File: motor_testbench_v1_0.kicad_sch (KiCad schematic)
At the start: 41 parts, among them IC1 PJA3402_R1_00001, J1 USB_C_Receptacle_USB2.0_16P, J3 Conn_02x06_Odd_Even, U1 ESP32-S3-WROOM-1, U3 ESP32-S3-DevKitC

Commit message: Add buffer OPA for Secondary battery measurement
[KiCad Version: 10.0.3]
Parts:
- removed J3: Conn_02x06_Odd_Even, Connector_PinHeader_2.00mm:PinHeader_2x06_P2.00mm_Vertical, symbol Connector_Generic:Conn_02x06_Odd_Even
- removed R56, R64, R65, R66: 22R, Resistor_SMD:R_0603_1608Metric_Pad0.98x0.95mm_HandSolder, symbol Device:R
- removed U3: ESP32-S3-DevKitC, custom_footprints:ESP32-S3-DevKitC_with_3DModel, symbol Espressif Symbols:ESP32-S3-DevKitC
- added C1, C134, C135, C5: 1u, Capacitor_SMD:C_0603_1608Metric_Pad1.08x0.95mm_HandSolder, symbol Device:C
- added C132: 10u, Capacitor_SMD:C_0603_1608Metric_Pad1.08x0.95mm_HandSolder, symbol Device:C
- added C6, C7, C8: 100n, Capacitor_SMD:C_0603_1608Metric_Pad1.08x0.95mm_HandSolder, symbol Device:C
- added D1, D2: GG040205170N2P, Diode_SMD:D_0402_1005Metric_Pad0.77x0.64mm_HandSolder, symbol Device:D
- added J2: Conn_02x08_Odd_Even, Connector_PinHeader_2.54mm:PinHeader_2x08_P2.54mm_Vertical, symbol Connector_Generic:Conn_02x08_Odd_Even
- added JP3: Jumper_2_Open, Jumper:SolderJumper-2_P1.3mm_Open_RoundedPad1.0x1.5mm, symbol Jumper:Jumper_2_Open
- added R1, R2: 5.1k, Resistor_SMD:R_0603_1608Metric_Pad0.98x0.95mm_HandSolder, symbol Device:R
- added R19, R20, R21, R3: 10k, Resistor_SMD:R_0603_1608Metric_Pad0.98x0.95mm_HandSolder, symbol Device:R
- added R73, R74: 22R, Resistor_SMD:R_0603_1608Metric_Pad0.98x0.95mm_HandSolder, symbol Device:R
- added SWd1, SWd4: SW_Push, Button_Switch_SMD:SW_SPST_TS-1088-xR020, symbol Switch:SW_Push
- added U21: OPA310SxDBV, Package_TO_SOT_SMD:SOT-23-6, symbol Amplifier_Operational:OPA310SxDBV
- renumbered C1 to C2, C2 to C3, C3 to C4, D1 to D3, R4 to R10, R59 to R11, R5 to R12, R7 to R14, R57 to R15, R67 to R16, R68 to R17, R69 to R18, R6 to R4, R60 to R5, R61 to R6, R1 to R7, R2 to R8, R3 to R9, SWd1 to SWd2, SWd2 to SWd3
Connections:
- net DS_ADC_MCLK is gone; now on net DS_ADC_IRQ: R15.2
- net +3V3_ESP: now also C5.1, J2.16 (Pin_16), R19.1, R20.1, R21.1, R3.1, U21.5 (~{SHDN})
- net ESP_EN/RST: now also SWd3.2, C7.1, R20.2
- net ESP_GPIO0: now also JP3.2 (B), R3.2, SWd4.2
- net ESP_GPIO1: now also C134.1, R74.2
- net ESP_GPIO11: now also J2.11 (Pin_11)
- net ESP_GPIO2: now also J2.15 (Pin_15)
- net ESP_GPIO38: now also J2.3 (Pin_3)
- net ESP_GPIO39: now also J2.2 (Pin_2)
- net ESP_GPIO40: now also J2.4 (Pin_4)
- net ESP_GPIO41: now also J2.6 (Pin_6)
- net ESP_GPIO42: now also J2.8 (Pin_8)
- net ESP_GPIO46: now also J2.9 (Pin_9)
- net ESP_GPIO9: now also C6.1, R19.2
- net ESP_UART_RX: now also J2.12 (Pin_12)
- net ESP_UART_TX: now also J2.10 (Pin_10)
- net ESP_USB_D+: now also D2.1 (K)
- net ESP_USB_D-: now also D1.1 (K)
- net GND: now also J1.SH (SHIELD), C1.2, C132.2, C134.2, C135.2, C5.2, C6.2, C7.2, C8.2, D1.2 (A), D2.2 (A), J2.1 (Pin_1), J2.14 (Pin_14), J2.5 (Pin_5), J2.7 (Pin_7), JP3.1 (A), R1.1, R2.1, SWd1.1, SWd4.1, U21.2 (V-)
- net V_secondary_Bat: now also U1.18 (IO10), C132.1, R73.2; no longer C4.1, R10.1, R9.2, U1.15 (IO3)
- net at J1.A4 (VBUS), J1.A9 (VBUS), J1.B4 (VBUS)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: now also C1.1
- net at J1.A5 (CC1): now also R1.2
- net at J1.B5 (CC2): now also R2.2
- removed net ESP_GPIO10: SWd3.2, U1.18 (IO10)
- new net: C4.1, R10.1, R9.2, U21.3 (+)
- new net: R73.1, U21.1, U21.4 (-)
- new net: J2.13 (Pin_13), R74.1
- new net +5V5_bus: C135.1, U21.6 (V+)
- new net ESP_GPIO3: C8.1, R21.2, SWd1.2, U1.15 (IO3)
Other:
- note added: "Extra Input Filter if ESP32 SAR ADC is used!"
- note added: "POISTA TAI TEE JOTAIN MCLK:LLE, EI VARMAAN TARVITA / EI VOI LAITTAA GPIO 45!"
- note added: "TARKASTA PINOUT: TLV9001SIDBVRG4"
- note removed: "ESP S3 DevKitC Header"
- moved on the sheet: C2, C3, C4, D3, J1, R10, R11, R12, R14, R15, R16, R17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

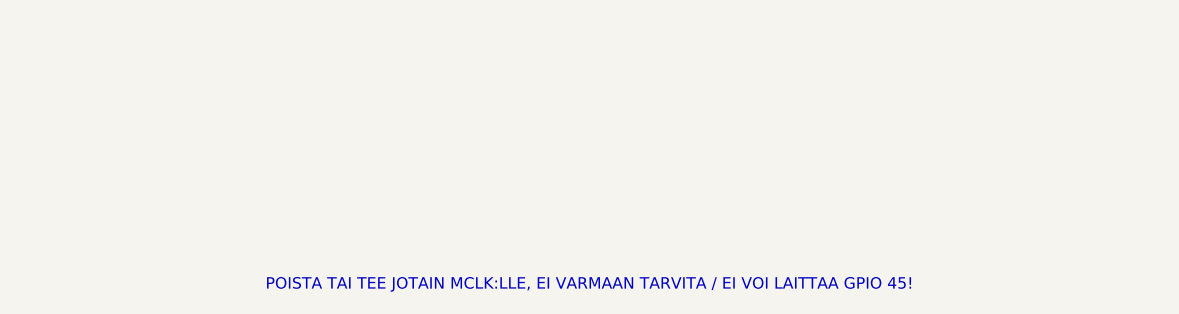
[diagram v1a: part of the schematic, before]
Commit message: Add LDO / Power sequencing for sensors
[KiCad Version: 10.0.3]
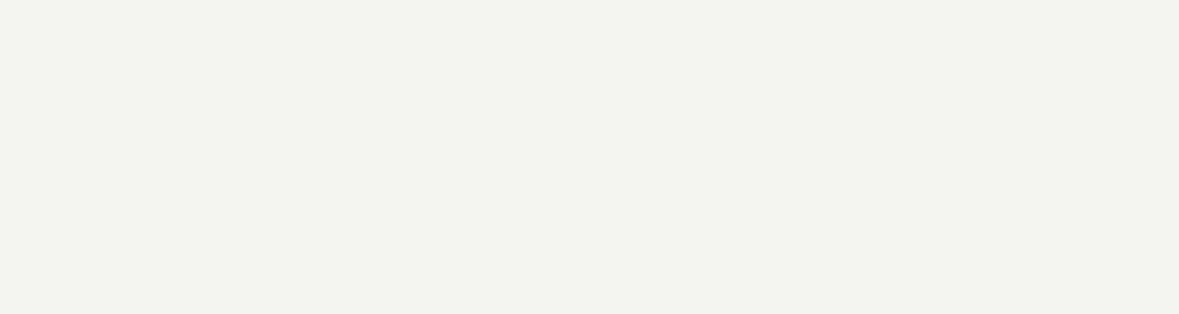
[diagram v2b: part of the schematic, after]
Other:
- note removed: "POISTA TAI TEE JOTAIN MCLK:LLE, EI VARMAAN TARVITA / EI VOI LAITTAA GPIO 45!"
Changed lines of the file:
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@@
-		)
-	)
-	(text "POISTA TAI TEE JOTAIN MCLK:LLE, EI VARMAAN TARVITA / EI VOI LAITTAA GPIO 45!"
-		(exclude_from_sim no)
-		(at 152.4 196.85 0)
-		(effects
-			(font
-				(size 1.27 1.27)
-			)
 		)
 	)

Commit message: Minor improvements. Add 3D model.
[KiCad Version: 10.0.4]
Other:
- moved on the sheet: C1, C132, C134, C135, C2, C3, C4, C5, C6, C7, C8, D1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

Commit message: Fix Via offset.
[KiCad Version: 10.0.4]
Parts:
- renumbered C2 to C1, C7 to C10, C8 to C11, C3 to C2, C5 to C3, C135 to C5, C1 to C6, C134 to C7, C132 to C8, C6 to C9, D3 to D1, D1 to D2, D2 to D3, JP3 to JP1, R3 to R1, R7 to R11, R16 to R12, R17 to R13, R18 to R14, R8 to R15, R1 to R16, R2 to R17, R74 to R18, R73 to R19, R4 to R2, R19 to R20, R20 to R21, R21 to R22, R5 to R3, R6 to R4, R11 to R5, R12 to R6, R14 to R7, R15 to R8, SWd4 to SWd1, SWd1 to SWd2, SWd2 to SWd3, SWd3 to SWd4, U21 to U2

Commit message: Minor improvements. Fix capacitor sizes.
[KiCad Version: 10.0.4]
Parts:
- removed H12, H9: MountingHole, MountingHole:MountingHole_2.2mm_M2_DIN965, symbol Mechanical:MountingHole
- added C3: 1u, Capacitor_SMD:C_0603_1608Metric_Pad1.08x0.95mm_HandSolder, symbol Device:C
- C5: renamed from C4; footprint Capacitor_SMD:C_0603_1608Metric_Pad1.08x0.95mm_HandSolder -> Capacitor_SMD:C_0805_2012Metric_Pad1.18x1.45mm_HandSolder
- C9: renamed from C8; footprint Capacitor_SMD:C_0603_1608Metric_Pad1.08x0.95mm_HandSolder -> Capacitor_SMD:C_0805_2012Metric_Pad1.18x1.45mm_HandSolder
- H1, H10, H11, H2, H3, H4, H5, H6, H7, H8: footprint MountingHole:MountingHole_2.2mm_M2_DIN965 -> MountingHole:MountingHole_3.2mm_M3
- IC1: footprint SOT95P240X110-3N -> SamacSys_Parts:SOT95P240X110-3N
- renumbered C9 to C10, C10 to C11, C11 to C12, C3 to C4, C5 to C6, C6 to C7, C7 to C8
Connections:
- net +3V3_ESP: now also J2.7 (Pin_7), C3.1
- net GND: now also C3.2; no longer J2.7 (Pin_7)
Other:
- moved on the sheet: C4

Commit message: PCB improvements.
[KiCad Version: 10.0.4]
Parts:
- removed J2: Conn_02x08_Odd_Even, Connector_PinHeader_2.54mm:PinHeader_2x08_P2.54mm_Vertical, symbol Connector_Generic:Conn_02x08_Odd_Even
- added J?: Conn_01x07_Pin, Connector_PinHeader_2.54mm:PinHeader_1x07_P2.54mm_Vertical, symbol Connector:Conn_01x07_Pin
- added J?: Conn_01x08_Pin, Connector_PinHeader_2.54mm:PinHeader_1x08_P2.54mm_Vertical, symbol Connector:Conn_01x08_Pin
- added TP (x3): TestPoint, TestPoint:TestPoint_Pad_D1.0mm, symbol Connector:TestPoint
- renumbered H11 to H10, H10 to H9
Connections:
- net +3V3_ESP: now also J?.5 (Pin_5), J?.8 (Pin_8)
- net ESP_GPIO11: now also J?.3 (Pin_3)
- net ESP_GPIO14: now also TP.1
- net ESP_GPIO2: now also J?.1 (Pin_1)
- net ESP_GPIO38: now also J?.7 (Pin_7)
- net ESP_GPIO39: now also J?.1 (Pin_1)
- net ESP_GPIO40: now also J?.2 (Pin_2)
- net ESP_GPIO41: now also J?.3 (Pin_3)
- net ESP_GPIO42: now also J?.4 (Pin_4)
- net ESP_GPIO46: now also J?.4 (Pin_4)
- net ESP_GPIO8: now also TP.1
- net ESP_UART_RX: now also J?.6 (Pin_6)
- net ESP_UART_TX: now also J?.5 (Pin_5)
- net GND: now also J?.6 (Pin_6), J?.7 (Pin_7), TP.1
- net at R18.1: now also J?.2 (Pin_2)
- no-connect marks 5 -> 6
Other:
- moved on the sheet: C3, C4

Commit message: PCB Improvements.
[KiCad Version: 10.0.4]
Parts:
- gave numbers to parts that had none: 2
- renumbered TP to TP1, TP to TP2, TP to TP3
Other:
- note added: "TODO: MAADOITA NÄMÄ?"
- note added: "TODO: TARKASTA PINOUT: TLV9001SIDBVRG4"
- note added: "TODO: VARMISTA ETTÄ PINNIT JA FOOTPRINT OIKEAT: PJA3402_R1_00001 SOT-23-3"
- note removed: "TARKASTA PINOUT: TLV9001SIDBVRG4"
- note removed: "VARMISTA ETTÄ PINNIT JA FOOTPRINT OIKEAT: PJA3402_R1_00001 SOT-23-3"
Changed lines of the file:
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@@
 		)
 	)
-	(text "Mechanical Mounting"
+	(text "TODO:\n\nVARMISTA ETTÄ PINNIT JA FOOTPRINT OIKEAT:\nPJA3402_R1_00001\nSOT-23-3\n"
 		(exclude_from_sim no)
-		(at 264.414 187.96 0)
+		(at 172.72 81.788 0)
 		(effects
 			(font
-				(size 1.27 1.27)
+				(size 1.905 1.905)
 			)
 		)
 	)
-	(text "TARKASTA PINOUT: TLV9001SIDBVRG4\n"
+	(text "Mechanical Mounting"
 		(exclude_from_sim no)
-		(at 220.98 62.23 0)
+		(at 264.414 187.96 0)
 		(effects
 			(font
@@
 		)
 	)
-	(text "VARMISTA ETTÄ PINNIT JA FOOTPRINT OIKEAT:\nPJA3402_R1_00001\nSOT-23-3\n"
+	(text "TODO: TARKASTA PINOUT: TLV9001SIDBVRG4\n"
 		(exclude_from_sim no)
-		(at 185.42 82.55 0)
+		(at 216.662 64.262 0)
 		(effects
 			(font
-				(size 1.27 1.27)
+				(size 1.905 1.905)
 			)
 		)
@@
 		)
 	)
+	(text "TODO: MAADOITA NÄMÄ?"
+		(exclude_from_sim no)
+		(at 277.622 215.9 0)
+		(effects
+			(font
+				(size 1.905 1.905)
+			)
+		)
+	)
 	(junction
 		(at 162.56 193.04)
@@
 		(dnp no)
 		(fields_autoplaced yes)
-		(property "Reference" "#PWR034"
+		(property "Reference" "#PWR035"
 			(at 264.16 130.81 0)
 			(hide yes)
@@
 			(project "motor_testbench_v1_0"
 				(path "/da638649-102c-44f9-b928-e91cd399cc2f"
-					(reference "#PWR034")
+					(reference "#PWR035")
 					(unit 1)
 				)
@@
 		(dnp no)
 		(fields_autoplaced yes)
-		(property "Reference" "#PWR026"
+		(property "Reference" "#PWR027"
 			(at 227.33 156.21 0)
 			(hide yes)
@@
 			(project "motor_testbench_v1_0"
 				(path "/da638649-102c-44f9-b928-e91cd399cc2f"
-					(reference "#PWR026")
+					(reference "#PWR027")
 					(unit 1)
 				)
@@
 		(in_pos_files yes)
 		(dnp no)
-		(property "Reference" "#PWR039"
+		(property "Reference" "#PWR040"
 			(at 280.67 147.32 0)
 			(hide yes)
@@
 			(project "motor_testbench_v1_0"
 				(path "/da638649-102c-44f9-b928-e91cd399cc2f"
-					(reference "#PWR039")
+					(reference "#PWR040")
 					(unit 1)
 				)
@@
 		(in_pos_files yes)
 		(dnp no)
-		(property "Reference" "TP"
+		(property "Reference" "TP2"
 			(at 41.91 158.75 0)
 			(hide yes)
@@
 			(project "motor_testbench_v1_0"
 				(path "/da638649-102c-44f9-b928-e91cd399cc2f"
-					(reference "TP")
+					(reference "TP2")
 					(unit 1)
 				)
@@
 		(in_pos_files yes)
 		(dnp no)
-		(property "Reference" "#PWR037"
+		(property "Reference" "#PWR038"
 			(at 280.67 113.03 0)
 			(hide yes)
@@
 			(project "motor_testbench_v1_0"
 				(path "/da638649-102c-44f9-b928-e91cd399cc2f"
-					(reference "#PWR037")
+					(reference "#PWR038")
 					(unit 1)
 				)
@@
 		(dnp no)
 		(fields_autoplaced yes)
-		(property "Reference" "#PWR016"
+		(property "Reference" "#PWR017"
 			(at 200.66 63.5 0)
 			(hide yes)
@@
 			(project "motor_testbench_v1_0"
 				(path "/da638649-102c-44f9-b928-e91cd399cc2f"
-					(reference "#PWR016")
+					(reference "#PWR017")
 					(unit 1)
 				)
@@
 		(in_pos_files yes)
 		(dnp no)
-		(property "Reference" "#PWR023"
+		(property "Reference" "#PWR024"
 			(at 223.52 55.88 0)
 			(hide yes)
@@
 			(project "motor_testbench_v1_0"
 				(path "/da638649-102c-44f9-b928-e91cd399cc2f"
-					(reference "#PWR023")
+					(reference "#PWR024")
 					(unit 1)
 				)
@@
 		(dnp no)
 		(fields_autoplaced yes)
-		(property "Reference" "J?"
+		(property "Reference" "J3"
 			(at 212.725 187.96 0)
 			(show_name no)
@@
 			(project "motor_testbench_v1_0"
 				(path "/da638649-102c-44f9-b928-e91cd399cc2f"
-					(reference "J?")
+					(reference "J3")
 					(unit 1)
 				)
@@
 		(in_pos_files yes)
 		(dnp no)
-		(property "Reference" "#PWR0247"
+		(property "Reference" "#PWR031"
 			(at 233.68 222.25 0)
 			(hide yes)
@@
 			(project "motor_testbench_v1_0"
 				(path "/da638649-102c-44f9-b928-e91cd399cc2f"
-					(reference "#PWR0247")
+					(reference "#PWR031")
 					(unit 1)
 				)
@@
 		(dnp no)
 		(fields_autoplaced yes)
-		(property "Reference" "#PWR036"
+		(property "Reference" "#PWR037"
 			(at 280.67 106.68 0)
 			(hide yes)
@@
 			(project "motor_testbench_v1_0"
 				(path "/da638649-102c-44f9-b928-e91cd399cc2f"
-					(reference "#PWR036")
+					(reference "#PWR037")
 					(unit 1)
 				)
@@
 		(in_pos_files yes)
 		(dnp no)
-		(property "Reference" "#PWR027"
+		(property "Reference" "#PWR028"
 			(at 227.33 273.05 0)
 			(hide yes)
@@
 			(project "motor_testbench_v1_0"
 				(path "/da638649-102c-44f9-b928-e91cd399cc2f"
-					(reference "#PWR027")
+					(reference "#PWR028")
 					(unit 1)
 				)
@@
 		(in_pos_files yes)
 		(dnp no)
-		(property "Reference" "#PWR013"
+		(property "Reference" "#PWR014"
 			(at 190.5 35.56 0)
 			(hide yes)
@@
 			(project "motor_testbench_v1_0"
 				(path "/da638649-102c-44f9-b928-e91cd399cc2f"
-					(reference "#PWR013")
+					(reference "#PWR014")
 					(unit 1)
 				)
@@
 		(in_pos_files yes)
 		(dnp no)
-		(property "Reference" "#PWR015"
+		(property "Reference" "#PWR016"
 			(at 191.77 279.4 0)
 			(hide yes)
@@
 			(project "motor_testbench_v1_0"
 				(path "/da638649-102c-44f9-b928-e91cd399cc2f"
-					(reference "#PWR015")
+					(reference "#PWR016")
 					(unit 1)
 				)
@@
 		(dnp no)
 		(fields_autoplaced yes)
-		(property "Reference" "#PWR038"
+		(property "Reference" "#PWR039"
 			(at 280.67 140.97 0)
 			(hide yes)
@@
 			(project "motor_testbench_v1_0"
 				(path "/da638649-102c-44f9-b928-e91cd399cc2f"
-					(reference "#PWR038")
+					(reference "#PWR039")
 					(unit 1)
 				)
@@
 		(dnp no)
 		(fields_autoplaced yes)
-		(property "Reference" "#PWR022"
+		(property "Reference" "#PWR023"
 			(at 223.52 44.45 0)
 			(hide yes)
@@
 			(project "motor_testbench_v1_0"
 				(path "/da638649-102c-44f9-b928-e91cd399cc2f"
-					(reference "#PWR022")
+					(reference "#PWR023")
 					(unit 1)
 				)
@@
 		(dnp no)
 		(fields_autoplaced yes)
-		(property "Reference" "#PWR033"
+		(property "Reference" "#PWR034"
 			(at 264.16 96.52 0)
 			(hide yes)
@@
 			(project "motor_testbench_v1_0"
 				(path "/da638649-102c-44f9-b928-e91cd399cc2f"
-					(reference "#PWR033")
+					(reference "#PWR034")
 					(unit 1)
 				)
@@
 		(in_pos_files yes)
 		(dnp no)
-		(property "Reference" "#PWR017"
+		(property "Reference" "#PWR013"
 			(at 187.96 218.44 0)
 			(hide yes)
@@
 			(project "motor_testbench_v1_0"
 				(path "/da638649-102c-44f9-b928-e91cd399cc2f"
-					(reference "#PWR017")
+					(reference "#PWR013")
 					(unit 1)
 				)
@@
 		(dnp no)
 		(fields_autoplaced yes)
-		(property "Reference" "#PWR032"
+		(property "Reference" "#PWR033"
 			(at 262.89 165.1 0)
 			(hide yes)
@@
 			(project "motor_testbench_v1_0"
 				(path "/da638649-102c-44f9-b928-e91cd399cc2f"
-					(reference "#PWR032")
+					(reference "#PWR033")
 					(unit 1)
 				)
@@
 		(dnp no)
 		(fields_autoplaced yes)
-		(property "Reference" "#PWR031"
+		(property "Reference" "#PWR032"
 			(at 240.03 63.5 0)
 			(hide yes)
@@
 			(project "motor_testbench_v1_0"
 				(path "/da638649-102c-44f9-b928-e91cd399cc2f"
-					(reference "#PWR031")
+					(reference "#PWR032")
 					(unit 1)
 				)
@@
 		(dnp no)
 		(fields_autoplaced yes)
-		(property "Reference" "J?"
+		(property "Reference" "J2"
 			(at 198.12 200.6599 0)
 			(show_name no)
@@
 			(project "motor_testbench_v1_0"
 				(path "/da638649-102c-44f9-b928-e91cd399cc2f"
-					(reference "J?")
+					(reference "J2")
 					(unit 1)
 				)
@@
 		(in_pos_files yes)
 		(dnp no)
-		(property "Reference" "#PWR025"
+		(property "Reference" "#PWR026"
 			(at 223.52 273.05 0)
 			(hide yes)
@@
 			(project "motor_testbench_v1_0"
 				(path "/da638649-102c-44f9-b928-e91cd399cc2f"
-					(reference "#PWR025")
+					(reference "#PWR026")
 					(unit 1)
 				)
@@
 		(in_pos_files yes)
 		(dnp no)
-		(property "Reference" "#PWR035"
+		(property "Reference" "#PWR036"
 			(at 280.67 78.74 0)
 			(hide yes)
@@
 			(project "motor_testbench_v1_0"
 				(path "/da638649-102c-44f9-b928-e91cd399cc2f"
-					(reference "#PWR035")
+					(reference "#PWR036")
 					(unit 1)
 				)
@@
 		(dnp no)
 		(fields_autoplaced yes)
-		(property "Reference" "#PWR040"
+		(property "Reference" "#PWR041"
 			(at 280.67 175.26 0)
 			(hide yes)
@@
 			(project "motor_testbench_v1_0"
 				(path "/da638649-102c-44f9-b928-e91cd399cc2f"
-					(reference "#PWR040")
+					(reference "#PWR041")
 					(unit 1)
 				)
@@
 		(in_pos_files yes)
 		(dnp no)
-		(property "Reference" "#PWR024"
+		(property "Reference" "#PWR025"
 			(at 223.52 250.19 0)
 			(hide yes)
@@
 			(project "motor_testbench_v1_0"
 				(path "/da638649-102c-44f9-b928-e91cd399cc2f"
-					(reference "#PWR024")
+					(reference "#PWR025")
 					(unit 1)
 				)
@@
 		(in_pos_files yes)
 		(dnp no)
-		(property "Reference" "TP"
+		(property "Reference" "TP3"
 			(at 236.22 213.36 0)
 			(hide yes)
@@
 			(project "motor_testbench_v1_0"
 				(path "/da638649-102c-44f9-b928-e91cd399cc2f"
-					(reference "TP")
+					(reference "TP3")
 					(unit 1)
 				)
@@
 		(in_pos_files yes)
 		(dnp no)
-		(property "Reference" "TP"
+		(property "Reference" "TP1"
 			(at 41.91 143.51 0)
 			(hide yes)
@@
 			(project "motor_testbench_v1_0"
 				(path "/da638649-102c-44f9-b928-e91cd399cc2f"
-					(reference "TP")
+					(reference "TP1")
 					(unit 1)
 				)
@@
 		(in_pos_files yes)
 		(dnp no)
-		(property "Reference" "#PWR028"
+		(property "Reference" "#PWR022"
 			(at 220.98 218.44 0)
 			(hide yes)
@@
 			(project "motor_testbench_v1_0"
 				(path "/da638649-102c-44f9-b928-e91cd399cc2f"
-					(reference "#PWR028")
+					(reference "#PWR022")
 					(unit 1)
 				)
@@
 		(dnp no)
 		(fields_autoplaced yes)
-		(property "Reference" "#PWR014"
+		(property "Reference" "#PWR015"
 			(at 190.5 63.5 0)
 			(hide yes)
@@
 			(project "motor_testbench_v1_0"
 				(path "/da638649-102c-44f9-b928-e91cd399cc2f"
-					(reference "#PWR014")
+					(reference "#PWR015")
 					(unit 1)
 				)
